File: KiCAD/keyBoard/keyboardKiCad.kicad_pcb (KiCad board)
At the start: 2 copper layers, 354 x 132 mm, 191 parts, among them SW1 RotaryEncoder_Switch_MP

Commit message: Gerber files generated, small touch ups to pass DRC. Ready for purchase.
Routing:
- net rotA: track 33.9 -> 28.6 mm
- net CHASSIS: track 977.0 -> 981.9 mm
- net rotC: track 34.5 -> 29.9 mm
- net rotB: track 36.2 -> 31.7 mm
- net rotSW: track 29.6 -> 25.9 mm, vias 1 -> 2
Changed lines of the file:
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@@
 			(outputformat 1)
 			(mirror no)
-			(drillshape 1)
+			(drillshape 0)
 			(scaleselection 1)
-			(outputdirectory "")
+			(outputdirectory "C:/Users/chith/Desktop/")
 		)
 	)
@@
 		(layer "F.Cu")
 		(transform
-			(translate 368 97)
+			(translate 363 99)
 			(rotate 0)
 			(scale 1 1)
@@
 		(layer "F.Cu")
 		(transform
-			(translate 355 91)
+			(translate 350 91)
 			(rotate 0)
 			(scale 1 1)
@@
 	)
 	(segment
-		(start 30 146.5)
-		(end 28.5 145)
+		(start 366.65 90.4)
+		(end 372 95.75)
 		(width 0.5)
 		(layer "F.Cu")
@@
 	)
 	(segment
-		(start 372 98.362742)
-		(end 372 115)
+		(start 30 146.5)
+		(end 28.5 145)
 		(width 0.5)
 		(layer "F.Cu")
@@
 	)
 	(segment
-		(start 364.637258 91)
-		(end 372 98.362742)
+		(start 372 95.75)
+		(end 372 115)
 		(width 0.5)
 		(layer "F.Cu")
@@
 	)
 	(segment
-		(start 229 88.5)
-		(end 299.301522 88.5)
+		(start 350 91)
+		(end 357.900406 91)
 		(width 0.5)
 		(layer "F.Cu")
@@
 	)
 	(segment
-		(start 355 91)
-		(end 364.637258 91)
+		(start 358.500406 90.4)
+		(end 366.65 90.4)
+		(width 0.5)
+		(layer "F.Cu")
+		(net "CHASSIS")
+	)
+	(segment
+		(start 229 88.5)
+		(end 299.301522 88.5)
 		(width 0.5)
 		(layer "F.Cu")
@@
 	)
 	(segment
-		(start 39.5 88.5)
-		(end 40.873 88.5)
+		(start 357.900406 91)
+		(end 358.500406 90.4)
 		(width 0.5)
 		(layer "F.Cu")
@@
 	)
 	(segment
-		(start 355 91)
-		(end 355 97)
+		(start 39.5 88.5)
+		(end 40.873 88.5)
 		(width 0.5)
-		(layer "B.Cu")
+		(layer "F.Cu")
 		(net "CHASSIS")
 	)
@@
 	)
 	(segment
-		(start 355 97)
+		(start 350 102)
 		(end 348 104)
 		(width 0.5)
@@
 	)
 	(segment
+		(start 350 91)
+		(end 350 102)
+		(width 0.5)
+		(layer "B.Cu")
+		(net "CHASSIS")
+	)
+	(segment
 		(start 355.5 113.5)
 		(end 344.5 102.5)
@@
 	)
 	(segment
-		(start 364.114 105.596)
-		(end 365.46 104.25)
-		(width 0.2)
-		(layer "F.Cu")
-		(net "rotA")
-	)
-	(segment
-		(start 342.5 90.5)
-		(end 357.596 105.596)
+		(start 341 87)
+		(end 342.5 88.5)
 		(width 0.2)
 		(layer "F.Cu")
@@
 	)
 	(segment
-		(start 341 87)
-		(end 342.5 88.5)
+		(start 358.25 106.25)
+		(end 360.46 106.25)
 		(width 0.2)
 		(layer "F.Cu")
@@
 	)
 	(segment
-		(start 357.596 105.596)
-		(end 364.114 105.596)
+		(start 342.5 90.5)
+		(end 358.25 106.25)
 		(width 0.2)
 		(layer "F.Cu")
@@
 	)
 	(segment
-		(start 357.363 105.923)
-		(end 341 89.56)
+		(start 341 89.56)
+		(end 358.94 107.5)
 		(width 0.2)
 		(layer "F.Cu")
@@
 	)
 	(segment
-		(start 368 104.25)
-		(end 366.327 105.923)
+		(start 361.75 107.5)
+		(end 363 106.25)
 		(width 0.2)
 		(layer "F.Cu")
@@
 	)
 	(segment
-		(start 366.327 105.923)
-		(end 357.363 105.923)
+		(start 358.94 107.5)
+		(end 361.75 107.5)
 		(width 0.2)
 		(layer "F.Cu")
@@
 	(segment
 		(start 343.097552 92.12)
-		(end 357.227552 106.25)
+		(end 358.804552 107.827)
 		(width 0.2)
 		(layer "F.Cu")
@@
 	)
 	(segment
-		(start 357.227552 106.25)
-		(end 368.54 106.25)
+		(start 358.804552 107.827)
+		(end 363.963 107.827)
 		(width 0.2)
 		(layer "F.Cu")
@@
 	)
 	(segment
-		(start 368.54 106.25)
-		(end 370.54 104.25)
+		(start 341 92.12)
+		(end 343.097552 92.12)
 		(width 0.2)
 		(layer "F.Cu")
@@
 	)
 	(segment
-		(start 341 92.12)
-		(end 343.097552 92.12)
+		(start 363.963 107.827)
+		(end 365.54 106.25)
 		(width 0.2)
 		(layer "F.Cu")
@@
 	)
 	(segment
-		(start 363.21 87.5)
-		(end 365.46 89.75)
+		(start 343.5 90)
+		(end 346 87.5)
 		(width 0.2)
 		(layer "F.Cu")
@@
 	)
 	(segment
-		(start 343.5 90)
-		(end 346 87.5)
+		(start 357 87.5)
+		(end 359 89.5)
 		(width 0.2)
 		(layer "F.Cu")
@@
 	(segment
 		(start 346 87.5)
-		(end 363.21 87.5)
+		(end 357 87.5)
 		(width 0.2)
 		(layer "F.Cu")
@@
 	)
 	(via
+		(at 359 89.5)
+		(size 0.6)
+		(drill 0.3)
+		(layers "F.Cu" "B.Cu")
+		(net "rotSW")
+	)
+	(via
 		(at 343.5 90)
 		(size 0.6)
@@
 	)
 	(segment
+		(start 360.46 90.96)
+		(end 360.46 91.75)
+		(width 0.2)
+		(layer "B.Cu")
+		(net "rotSW")
+	)
+	(segment
 		(start 341 94.68)
 		(end 343.5 92.18)
@@
 		(net "rotSW")
 	)
+	(segment
+		(start 359 89.5)
+		(end 360.46 90.96)
+		(width 0.2)
+		(layer "B.Cu")
+		(net "rotSW")
+	)
 	(via
 		(at 370.5 210)
@@
 	)
 	(via
-		(at 311.5 95.25)
+		(at 311.452859 95.325865)
 		(size 0.6)
 		(drill 0.3)

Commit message: Removed star point grounding on Hector's advice.
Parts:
- removed REF**: MountingHole_3.2mm_M3_Pad, MountingHole:MountingHole_3.2mm_M3_Pad
- removed REF**: NetTie-2_THT_Pad0.3mm, NetTie:NetTie-2_THT_Pad0.3mm
- added ?: , , F.Cu at (0.00, 0.00)
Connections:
- ? pad 1: CHASSIS -> GND (x17)
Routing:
- net CHASSIS: track 981.9 -> 0.00 mm

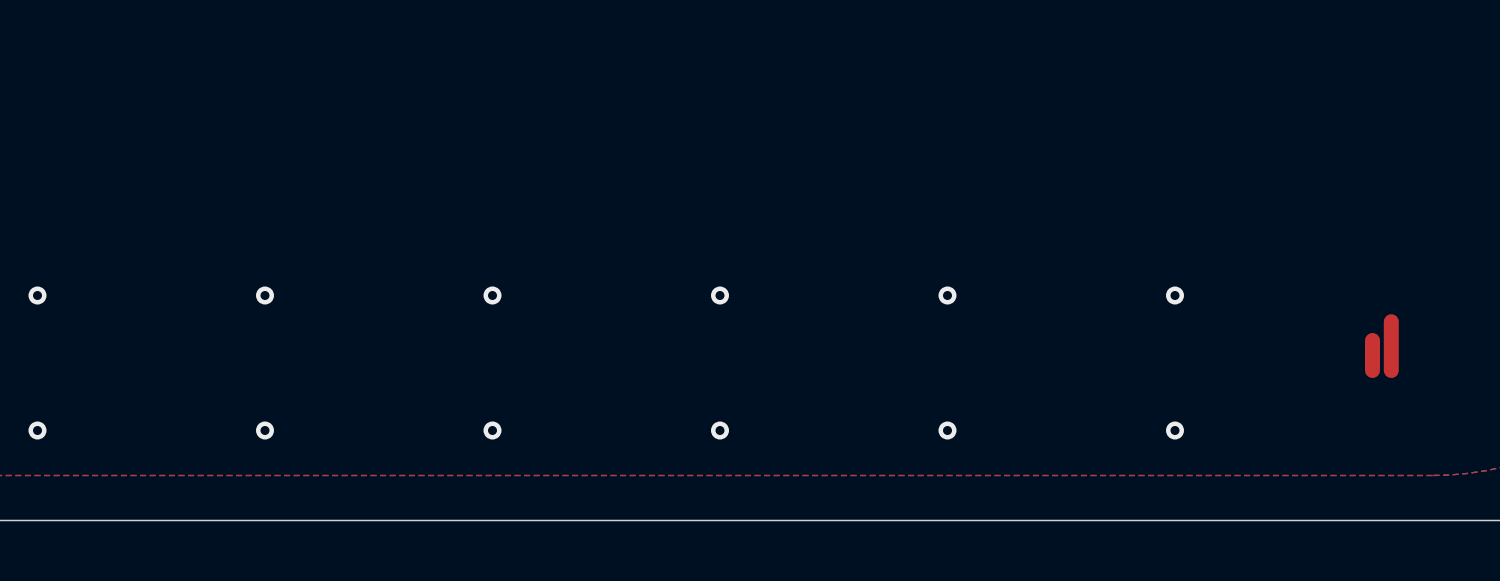
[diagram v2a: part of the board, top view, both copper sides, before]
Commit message: Added silly logo, regenerated gerber
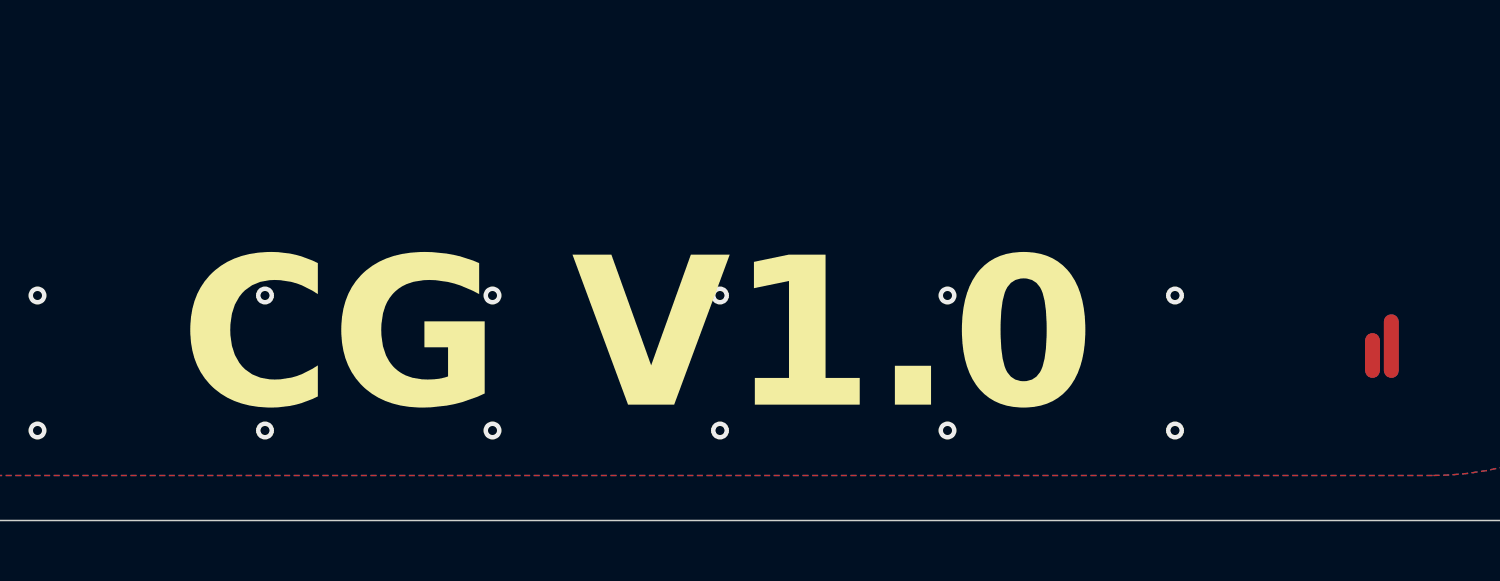
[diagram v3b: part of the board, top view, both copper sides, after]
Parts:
- added G***: LOGO, LOGO, B.Cu at (0.00, 0.00)
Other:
- board text added: "CG V1.0"
